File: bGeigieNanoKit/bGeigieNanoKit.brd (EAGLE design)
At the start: 104.8 x 66.7 mm, 38 parts, among them T1 2SC1815

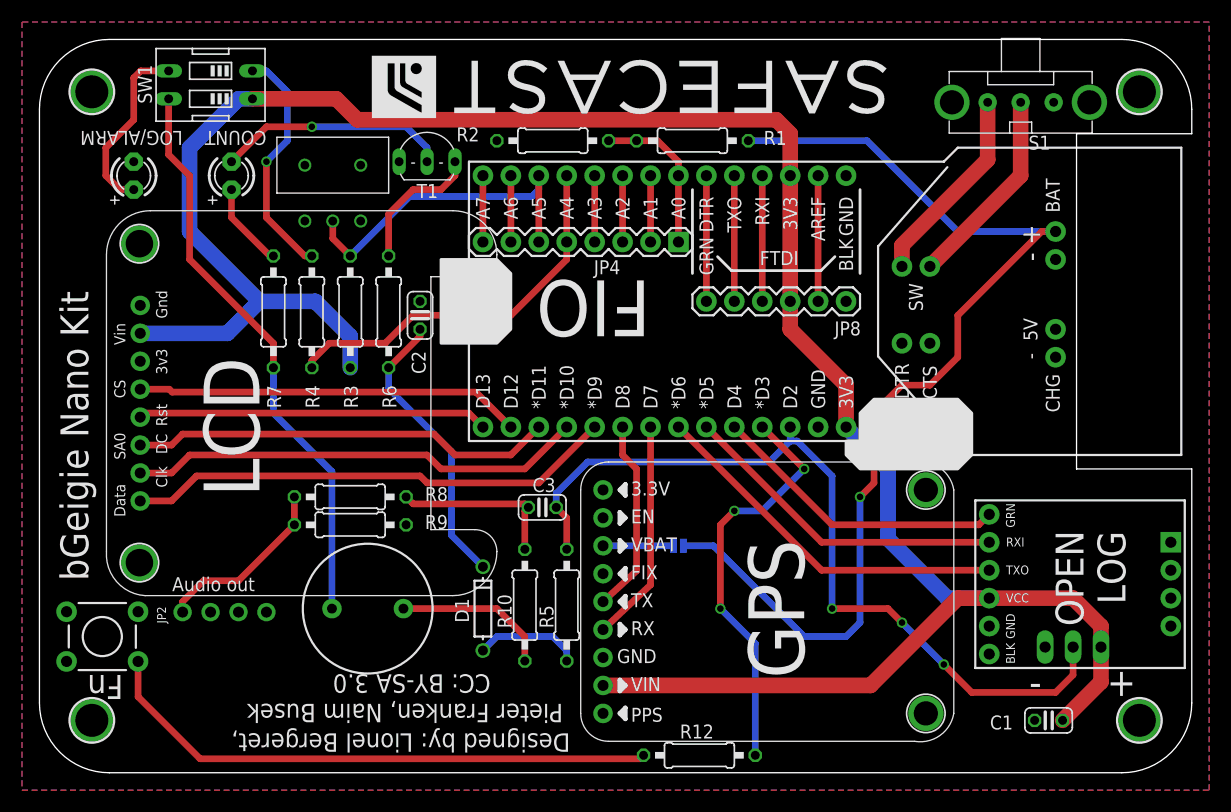
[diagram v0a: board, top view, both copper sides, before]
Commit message: Changed R8 to 47k and and R9 to 4.7k and fixed some overlaying text.
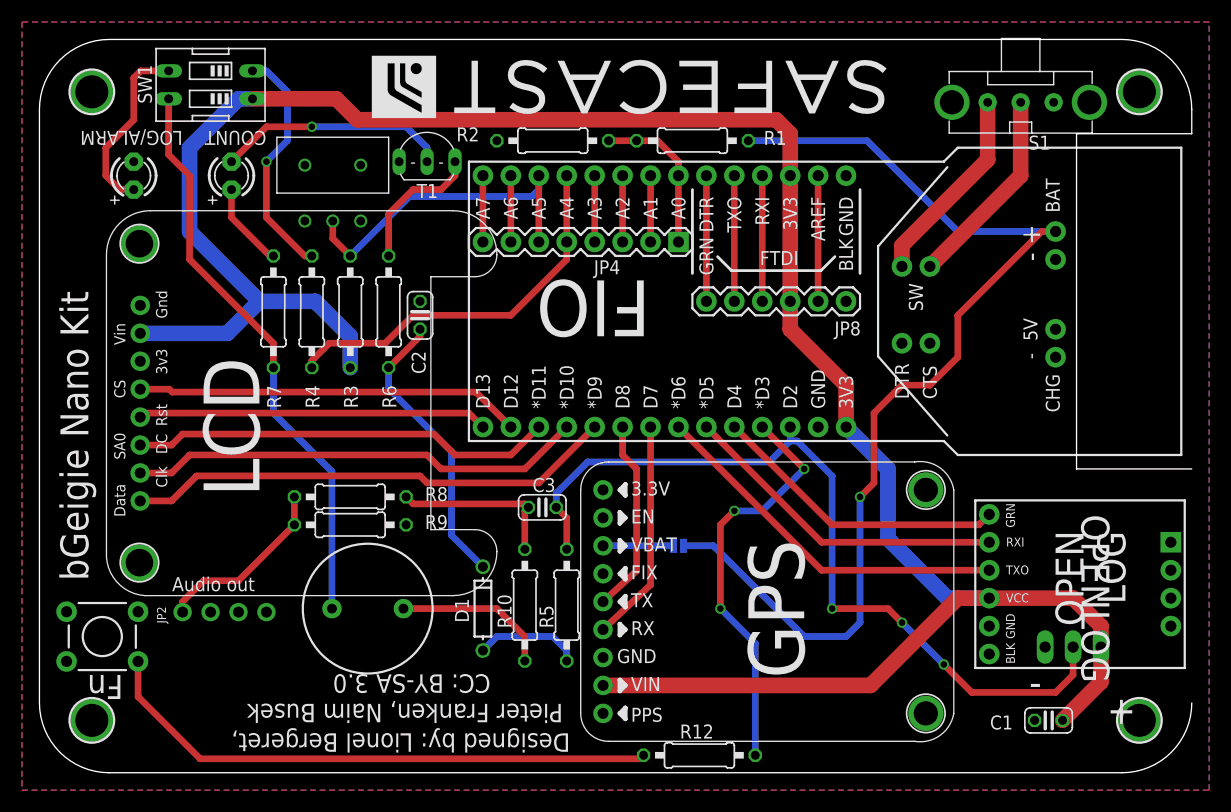
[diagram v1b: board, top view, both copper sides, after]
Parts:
- R7: value 51 Ohm -> 51
- R8: value 10k -> 47k
- R9: value 2.2k -> 4.7k
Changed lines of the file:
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@@
 <layer number="220" name="220bmp" color="21" fill="1" visible="no" active="no"/>
 <layer number="221" name="221bmp" color="22" fill="1" visible="no" active="no"/>
+<layer number="222" name="222bmp" color="23" fill="1" visible="no" active="no"/>
 <layer number="223" name="223bmp" color="24" fill="1" visible="no" active="no"/>
 <layer number="224" name="224bmp" color="25" fill="1" visible="no" active="no"/>
@@
 <wire x1="7.9375" y1="1.5875" x2="100.0125" y2="1.5875" width="0" layer="20"/>
 <wire x1="100.0125" y1="1.5875" x2="106.3625" y2="7.9375" width="0" layer="20" curve="90"/>
-<wire x1="106.3625" y1="7.9375" x2="106.3625" y2="29.21" width="0" layer="20"/>
 <wire x1="106.3625" y1="29.21" x2="95.885" y2="29.21" width="0" layer="20"/>
 <wire x1="95.885" y1="29.21" x2="95.885" y2="59.69" width="0" layer="20"/>
@@
 <text x="71.12" y="10.16" size="5.08" layer="21" font="vector" ratio="10" rot="R90">GPS</text>
 <text x="13.6525" y="18.0975" size="1.27" layer="21" font="vector" ratio="10" rot="SR0">Audio out</text>
-<text x="101.2825" y="11.1125" size="2.54" layer="21" font="vector" ratio="10" rot="R180">+</text>
+<text x="101.2825" y="8.5725" size="2.54" layer="21" font="vector" ratio="10" rot="R180">+</text>
 <text x="92.71" y="11.1125" size="2.54" layer="21" font="vector" ratio="10" rot="R180">-</text>
-<text x="92.075" y="8.5725" size="2.54" layer="22" font="vector" ratio="10" rot="MR0">-</text>
 <text x="100.6475" y="8.5725" size="2.54" layer="22" font="vector" ratio="10" rot="MR0">+</text>
 <text x="81.915" y="66.675" size="1.27" layer="22" font="vector" ratio="10" distance="60" rot="MR0" align="top-left">Special thanks to: Joe,Rob,Jurgen,Sean,Robin,Akiba,Azby
@@
 <text x="6.0325" y="19.05" size="2.54" layer="21" font="vector" ratio="10" distance="40" rot="R90">bGeigie Nano Kit</text>
 <text x="9.2075" y="10.4775" size="2.1844" layer="21" font="vector" ratio="9" rot="SR180">Fn</text>
-<polygon width="0.254" layer="21">
-<vertex x="76.2" y="34.29"/>
-<vertex x="77.47" y="35.56"/>
-<vertex x="85.09" y="35.56"/>
-<vertex x="86.36" y="34.29"/>
-<vertex x="86.36" y="30.48"/>
-<vertex x="85.09" y="29.21"/>
-<vertex x="76.2" y="29.21"/>
-<vertex x="74.93" y="30.48"/>
-<vertex x="74.93" y="31.75"/>
-<vertex x="76.2" y="31.75"/>
-</polygon>
-<polygon width="0.254" layer="21">
-<vertex x="38.1" y="48.26"/>
-<vertex x="43.18" y="48.26"/>
-<vertex x="44.45" y="46.99"/>
-<vertex x="44.45" y="41.91"/>
-<vertex x="43.18" y="40.64"/>
-<vertex x="38.1" y="40.64"/>
-</polygon>
 <text x="7.9375" y="58.1025" size="2.54" layer="22" font="vector" ratio="10" distance="40" rot="SMR270">bGeigie Nano Kit v1.0r2</text>
 </plain>
@@
 <attribute name="VALUE" x="33.9725" y="41.2369" size="1.27" layer="27" ratio="10" rot="R90"/>
 </element>
-<element name="R7" library="rcl" package="0207/10" value="51 Ohm" x="22.86" y="43.4975" smashed="yes" rot="R90">
+<element name="R7" library="rcl" package="0207/10" value="  51" x="22.86" y="43.4975" smashed="yes" rot="R90">
 <attribute name="NAME" x="23.5585" y="34.7345" size="1.27" layer="25" ratio="10" rot="R90"/>
 <attribute name="VALUE" x="23.495" y="39.9669" size="1.27" layer="27" ratio="10" rot="R90"/>
 </element>
-<element name="R8" library="rcl" package="0207/10" value="10k" x="29.845" y="26.67" smashed="yes">
+<element name="R8" library="rcl" package="0207/10" value="47k" x="29.845" y="26.67" smashed="yes">
 <attribute name="NAME" x="36.6395" y="26.289" size="1.27" layer="25" ratio="10"/>
 <attribute name="VALUE" x="28.2194" y="26.035" size="1.27" layer="27" ratio="10"/>
 </element>
-<element name="R9" library="rcl" package="0207/10" value="2.2k" x="29.845" y="24.13" smashed="yes">
+<element name="R9" library="rcl" package="0207/10" value="4.7k" x="29.845" y="24.13" smashed="yes">
 <attribute name="NAME" x="36.6395" y="23.749" size="1.27" layer="25" ratio="10"/>
 <attribute name="VALUE" x="30.8356" y="24.765" size="1.27" layer="27" ratio="10" rot="R180"/>
@@
 <attribute name="VALUE" x="34.29" y="53.848" size="1.27" layer="27" ratio="10" display="off"/>
 </element>
-<element name="OPENLOG" library="open_hw_sockets" package="OPENLOG" value="OPENLOG" x="86.6775" y="26.3525" smashed="yes" rot="R270">
-<attribute name="NAME" x="96.3295" y="25.0825" size="2.54" layer="25" rot="SR270" display="off"/>
-</element>
+<element name="OPENLOG" library="open_hw_sockets" package="OPENLOG" value="OPENLOG" x="86.6775" y="26.3525" rot="R270"/>
 <element name="SW1" library="special" package="EDG-02" value="" x="17.145" y="64.135" smashed="yes" rot="SR90">
 <attribute name="VALUE" x="23.749" y="60.833" size="1.27" layer="27" ratio="10" rot="SR90"/>
